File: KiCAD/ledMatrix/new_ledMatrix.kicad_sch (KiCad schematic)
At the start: 74 parts

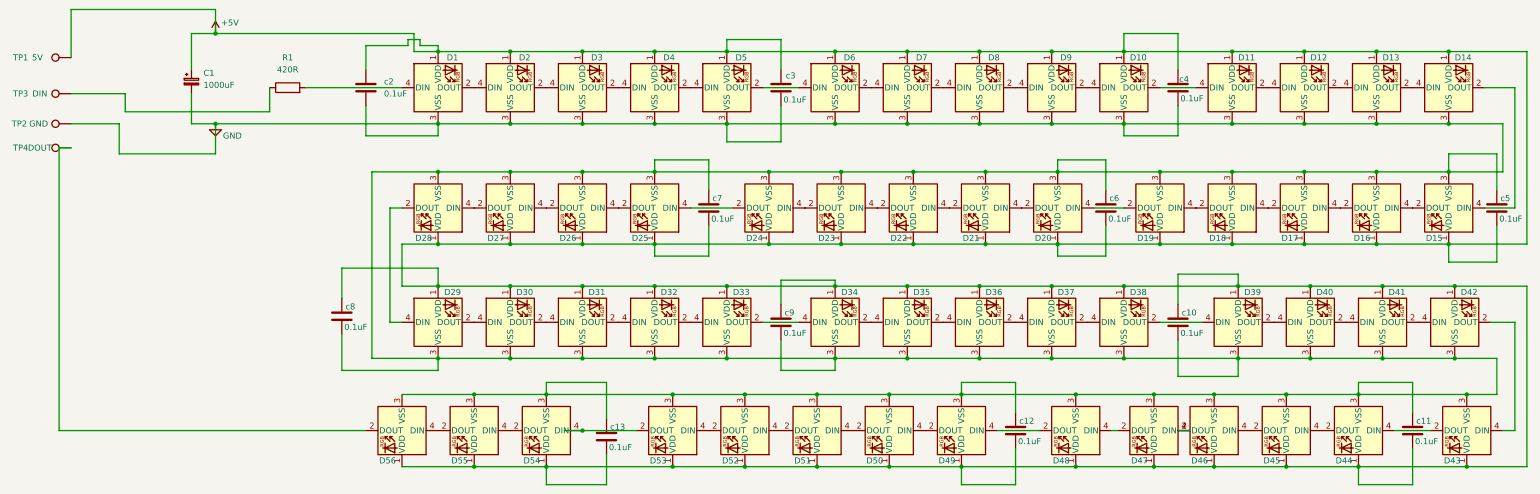
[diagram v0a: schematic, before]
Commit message: Cleanup: keep single source STL/KiCad files; remove duplicates
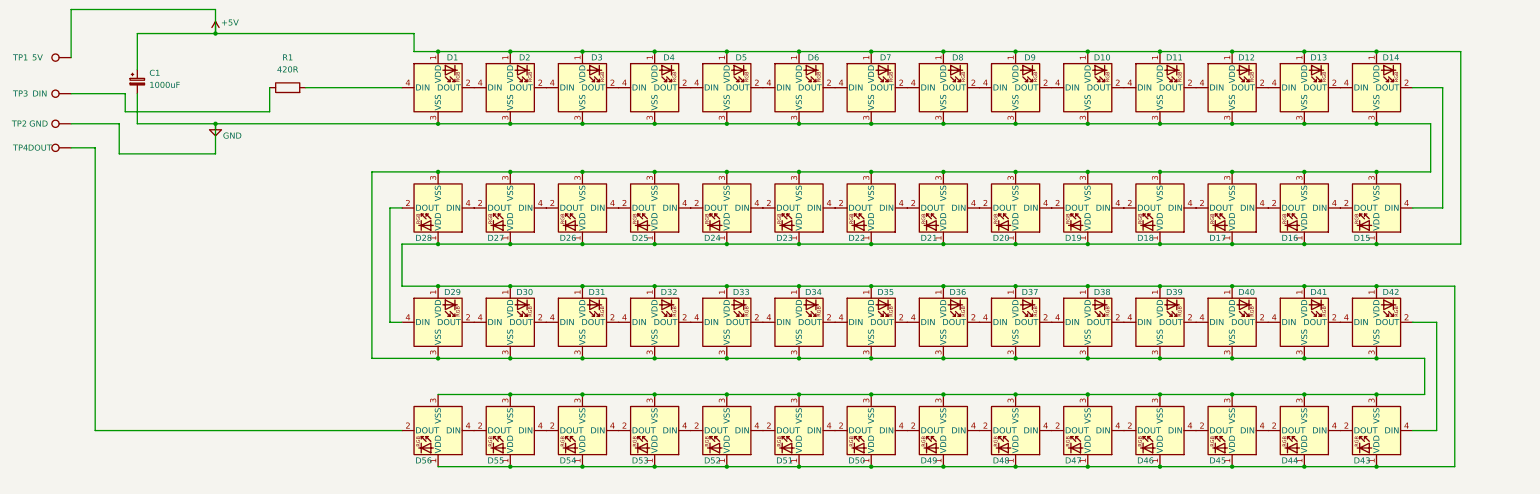
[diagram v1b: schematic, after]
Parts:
- removed c10, c11, c12, c13, c2, c3, c4, c5, c6, c7, c8, c9: 0.1uF, Capacitor_SMD:C_0603_1608Metric, symbol Device:C
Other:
- moved on the sheet: C1, D10, D11, D12, D13, D14, D15, D16, D17, D18, D19, D20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
